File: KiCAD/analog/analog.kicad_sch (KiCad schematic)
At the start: 0 parts

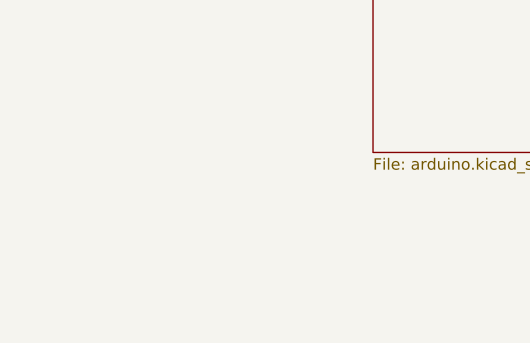
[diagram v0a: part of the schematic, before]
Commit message: revD analog: DGFET op-amp offset-mute topology + doc updates
Retire the Q11/Q12 PNP KeyUp mute path on the DGFET keyer G2 (sim showed
only ~2.6:1 on/off ratio with G1 biased above V_TO). Replace with an
LM7171 (U10) non-inverting op-amp wired as DC offset:
  V_G2 = V_DAC * (1 + R20/R23) - V_ref * (R20/R23)
with V_ref ~5.05V (1N4733A Zener D2, R24 1K bias, R25 1K / R32 100K
summing divider) and R20=6.2K / R23=10K (G=0.62). DAC=0 drives G2 to
-3.1V (fully cuts off the 40673, sim-verified 12pA leakage, ~10^9 on/off
ratio); DAC=5V drives G2 to +5V (matches prior keyed operating point).
KEY_UP net eliminated -- mute is intrinsic to the signal path, firmware
controls RF enable/disable solely via what it writes to the MCP4921
envelope channel.

Includes new test.kicad_sch sheet carrying the U10/R20-R32 subcircuit.

Doc updates: CLAUDE.md DGFET section rewritten; handoff doc gets a new
"DGFET keyer mute topology" section explaining retirement reason and
new transfer function; Master_Description Sec 2 and SPI-bus section
updated; revD_interconnect G2 amplitude-control block updated;
control_board_functional_blocks.md gets a prominent retirement banner
pointing at the current scheme.

Co-Authored-By: Claude Opus 4.7 <noreply@anthropic.com>
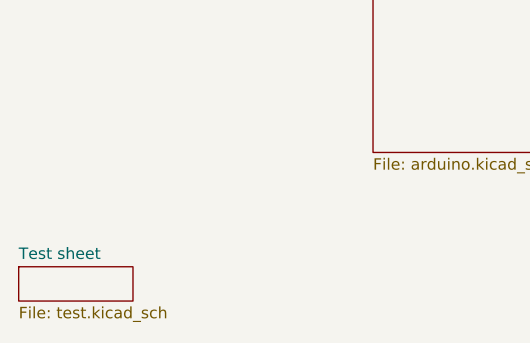
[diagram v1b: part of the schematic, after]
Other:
- added sheet Test sheet (test.kicad_sch)
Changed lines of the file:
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@@
 	(paper "A4")
+	(sheet
+		(at 50.8 157.48)
+		(size 12.7 3.81)
+		(exclude_from_sim no)
+		(in_bom yes)
+		(on_board yes)
+		(dnp no)
+		(fields_autoplaced yes)
+		(stroke
+			(width 0.1524)
+			(type solid)
+		)
+		(fill
+			(color 0 0 0 0)
+		)
+		(property "Sheetname" "Test sheet"
+			(at 50.8 156.7684 0)
+			(show_name no)
+			(do_not_autoplace no)
+			(effects
+				(font
+					(size 1.27 1.27)
+				)
+				(justify left bottom)
+			)
+		)
+		(property "Sheetfile" "test.kicad_sch"
+			(at 50.8 161.8746 0)
+			(show_name no)
+			(do_not_autoplace no)
+			(effects
+				(font
+					(size 1.27 1.27)
+				)
+				(justify left top)
+			)
+		)
+		(instances
+			(project "analog"
+				(path "/d3de40b8-856b-4fbd-829c-f45ffcd55742"
+					(page "4")
+				)
+			)
+		)
+	)
 	(sheet
 		(at 90.17 106.68)

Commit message: revD: analog + ss_pa RF filtering on umbilical signals
ss_pa: 1 uH RFC + bypass cap(s) added on each umbilical-crossing signal
to attenuate 14 MHz ingress from the cable and keep hot IRF510-source
RF from being injected back into the umbilical:

- PA_Bias_A_Raw: L6 1uH + C13 100nF + C26 100pF at J31.7
- PA_Bias_B_Raw: L7 1uH + C22 100nF + C27 100pF at J31.8
- Source_Sense_A: L8 1uH + C23 100nF between IRF510A source tap and
  the shared comparator/ADC node (new Source_Sense_A_Raw holds the
  Kelvin sense resistors R1/R2)
- Source_Sense_B: L9 1uH + C24 100nF, mirror of A on Q4 side
- DRIVER_BIAS: R20 100R + C19 0.1uF + C20 100pF already placed
  previously
- FAULT_N: R23 100R + C25 100pF filter on the external side of the
  latch (LM393 outputs + R9 pullup remain on the internal node for
  fast latching, R23 isolates from umbilical and 4066 enables)

Attenuation ~40-60 dB at 14 MHz across all five umbilical signals.

Analog: companion schematic touches for the DGFET G2 op-amp mute
subcircuit on the test sheet.

Co-Authored-By: Claude Opus 4.7 <noreply@anthropic.com>
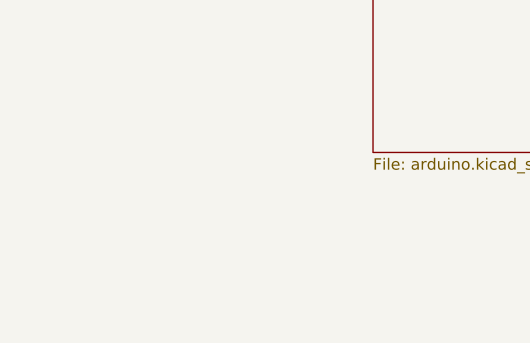
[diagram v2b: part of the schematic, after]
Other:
- removed sheet Test sheet
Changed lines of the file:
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@@
 	(paper "A4")
-	(sheet
-		(at 50.8 157.48)
-		(size 12.7 3.81)
-		(exclude_from_sim no)
-		(in_bom yes)
-		(on_board yes)
-		(dnp no)
-		(fields_autoplaced yes)
-		(stroke
-			(width 0.1524)
-			(type solid)
-		)
-		(fill
-			(color 0 0 0 0)
-		)
-		(property "Sheetname" "Test sheet"
-			(at 50.8 156.7684 0)
-			(show_name no)
-			(do_not_autoplace no)
-			(effects
-				(font
-					(size 1.27 1.27)
-				)
-				(justify left bottom)
-			)
-		)
-		(property "Sheetfile" "test.kicad_sch"
-			(at 50.8 161.8746 0)
-			(show_name no)
-			(do_not_autoplace no)
-			(effects
-				(font
-					(size 1.27 1.27)
-				)
-				(justify left top)
-			)
-		)
-		(instances
-			(project "analog"
-				(path "/d3de40b8-856b-4fbd-829c-f45ffcd55742"
-					(page "4")
-				)
-			)
-		)
-	)
 	(sheet
 		(at 90.17 106.68)
